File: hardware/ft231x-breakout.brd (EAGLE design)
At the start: 26.7 x 15.2 mm, 27 parts, among them Q1 2N7002PW, U1 FTS31XS-U

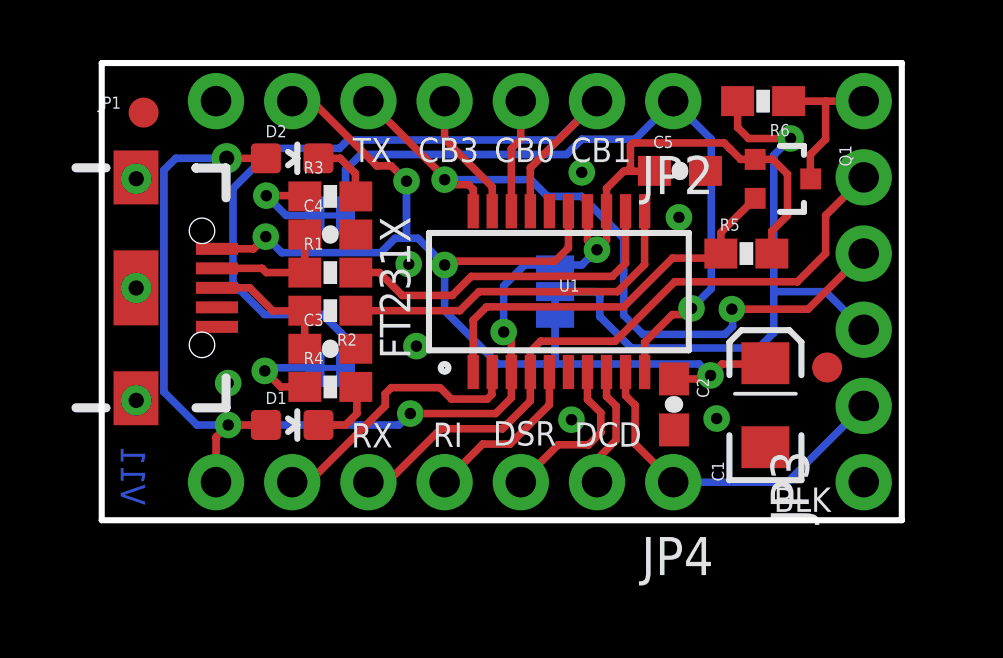
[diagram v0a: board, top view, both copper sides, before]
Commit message: Changed PCB dimension
Increased PCB dimension to better support USB connector.  Also slightly
adjusted the connector location itself to sit correctly on the PCB edge.
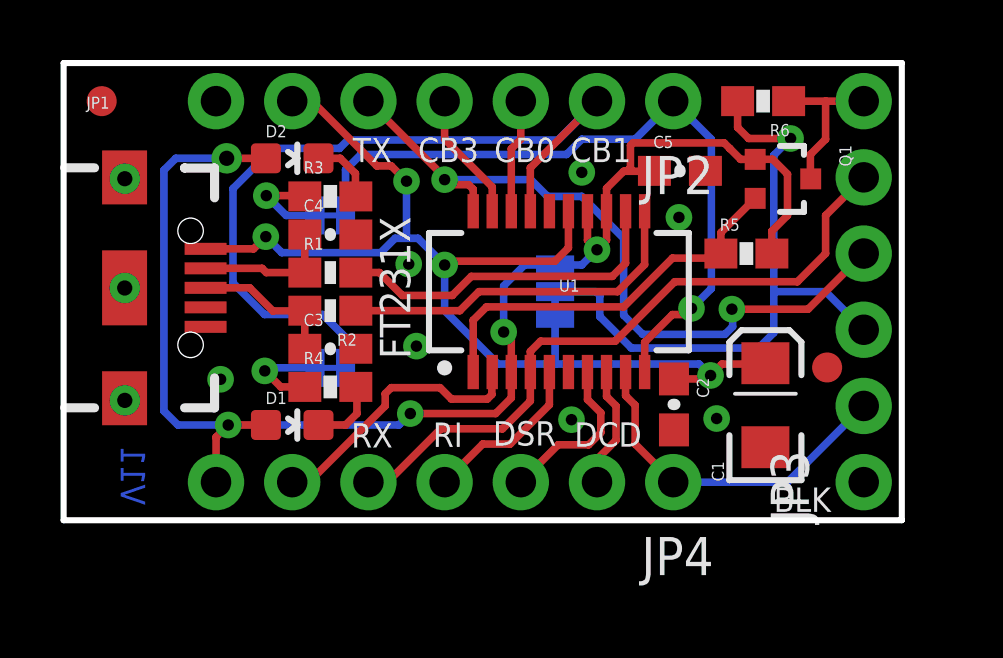
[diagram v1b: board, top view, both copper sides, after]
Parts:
- D2: value YELLOW -> Yellow
- JP2, JP4: device SparkFun-Connectors:1X07_NS -> SparkFun-Connectors:1X07_NO_SILK
- JP3: device SparkFun-Connectors:1X06_NS -> SparkFun-Connectors:1X06_NO_SILK
- R3, R4, R5, R6: device SparkFun-Resistors:0603-RES -> SparkFun-Resistors:0603-RES@1
- moved JP6 1.45 mm to (0.00, 14.0)
- moved JP1 0.38 mm to (0.76, 7.75)
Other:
- board size 26.7 x 15.2 mm -> 27.9 x 15.2 mm

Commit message: Moved design to 0,0 on grid and v number
Per QC review: moved design to 0 of XY grid in brd file and moved
version number to edge of board.
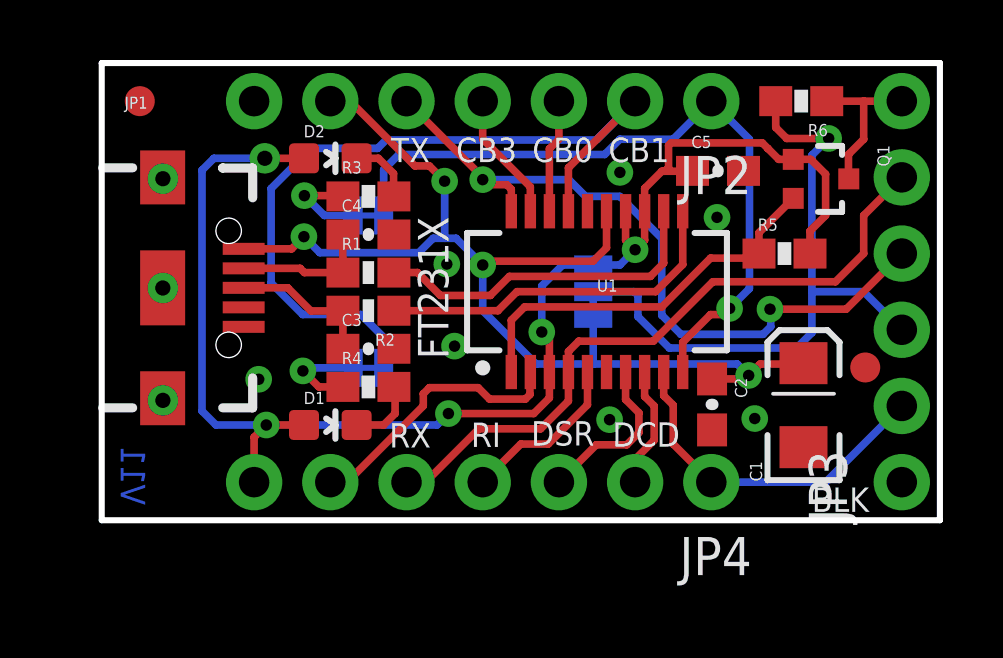
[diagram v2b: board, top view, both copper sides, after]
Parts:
- moved C2 1.27 mm to (20.3, 3.86)
- moved JP3 1.27 mm to (26.7, 1.27)
- moved R5 1.27 mm to (22.8, 8.89)
- moved LOGO1 1.27 mm to (14.0, 5.59)
- moved U1 1.27 mm to (16.5, 7.62)
- moved C3 1.27 mm to (8.89, 5.71)
- moved C4 1.27 mm to (8.89, 9.53)
- moved D1 1.27 mm to (7.62, 3.17)
- moved D2 1.27 mm to (7.62, 12.1)
- moved R1 1.27 mm to (8.89, 8.26)
- moved R2 1.27 mm to (8.89, 6.99)
- moved R3 1.27 mm to (8.89, 10.8)
- moved R4 1.27 mm to (8.89, 4.45)
- moved SJ2 1.27 mm to (8.89, 10.2)
- moved SJ3 1.27 mm to (8.89, 5.08)
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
